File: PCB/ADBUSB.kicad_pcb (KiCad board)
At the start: 2 copper layers, 36.2 x 36 mm, 6 parts, among them J1 MLD-MDC-4-02, J2 MLD-MDC-4-02, SW1 SW_Slide_DPDT SHOU HAN MSK-22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, U1 ProMicro

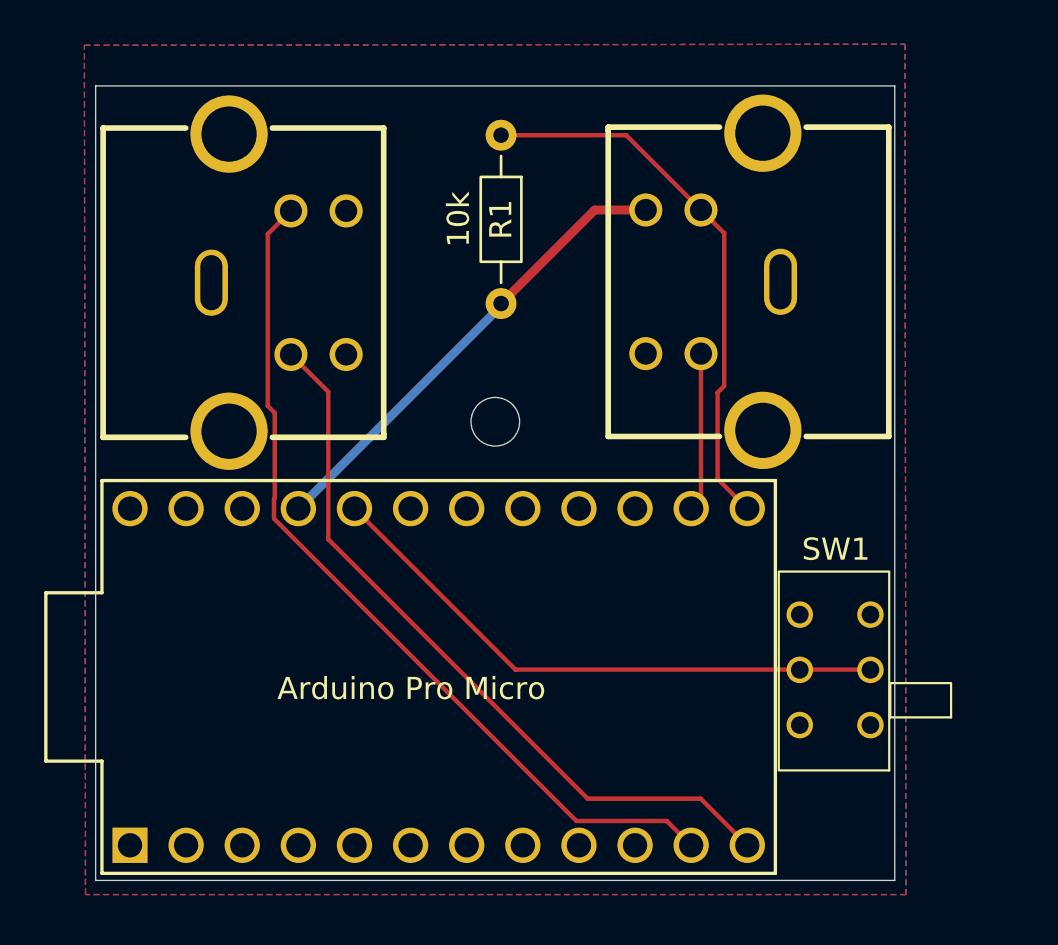
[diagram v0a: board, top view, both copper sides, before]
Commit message: Update for diode, pushbutton, raw
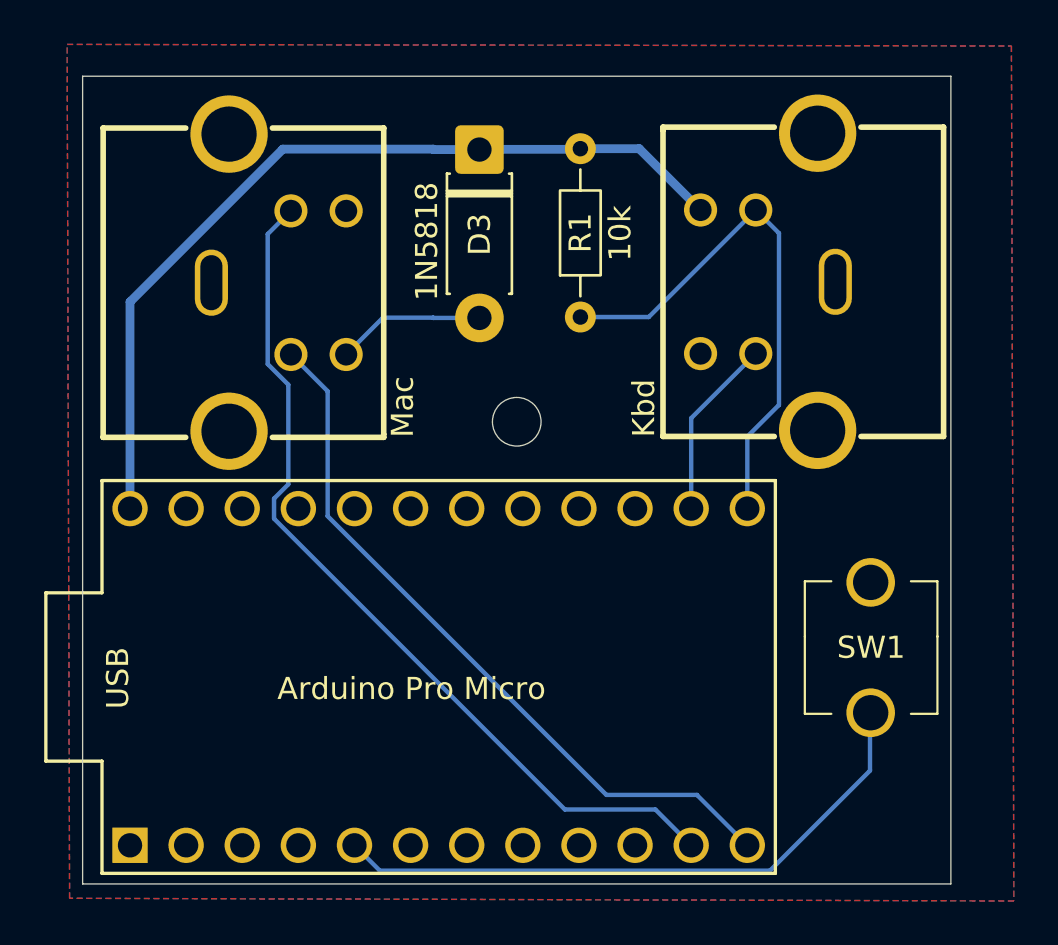
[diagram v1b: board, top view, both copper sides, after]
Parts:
- added D3: 1N5818, Diode_THT:D_DO-41_SOD81_P7.62mm_Horizontal, F.Cu at (155.5, 63.8)
- SW1: value SW_Slide_DPDT SHOU HAN MSK-22D18G4 051 -> SW_SPST; footprint DIN5:DPDT slide switch C7507433 -> Pushbutton:SPST_power_switch_horizontal
- moved R1 8.98 mm to (160.1, 71.4), turned to 90 degrees
- moved SW1 4.04 mm to (173.7, 85.8), turned to -90 degrees
- moved J2 2.48 mm to (171.5, 69.6)
- moved REF** 0.97 mm to (157.2, 76.1)
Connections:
- J1 pad 3: unconnected-(J1-Pad3) -> Net-(D3-A)
- J2 pad 3: VCC -> RAW_5V
- R1 pad 2: VCC -> RAW_5V
- SW1 pad 1: GND -> Net-(U1-SDA)
- SW1 pad 2: Net-(U1-F4) -> GND
- U1 pad 20: Net-(U1-F4) -> unconnected-(U1-F4-Pad20)
- U1 pad 21: VCC -> unconnected-(U1-VCC-Pad21)
- U1 pad 24: unconnected-(U1-RAW-Pad24) -> RAW_5V
- U1 pad 5: unconnected-(U1-SDA-Pad5) -> Net-(U1-SDA)
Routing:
- net RAW_5V: track 0.00 -> 39.2 mm
- net Net-(U1-SDA): track 0.00 -> 28.3 mm
- net Net-(U1-F4): track 26.4 -> 0.00 mm
- net VCC: track 21.4 -> 0.00 mm
- net Net-(D3-A): track 0.00 -> 6.73 mm
- net Net-(U1-B2): track 7.20 -> 8.23 mm
- net Net-(U1-B5): track 34.1 -> 33.5 mm
- net Net-(U1-B6): track 25.1 -> 24.5 mm
- net Net-(U1-B4): track 39.9 -> 40.4 mm
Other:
- board size 36.2 x 36 mm -> 39.3 x 36.6 mm
- board text added: "Kbd"
- board text added: "Mac"
- board text added: "USB"
